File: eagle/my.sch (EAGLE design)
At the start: 15 parts, among them U1 ESP8266-01, U2 AM2301, U3 PIC12F675P, U4 U1V11F3

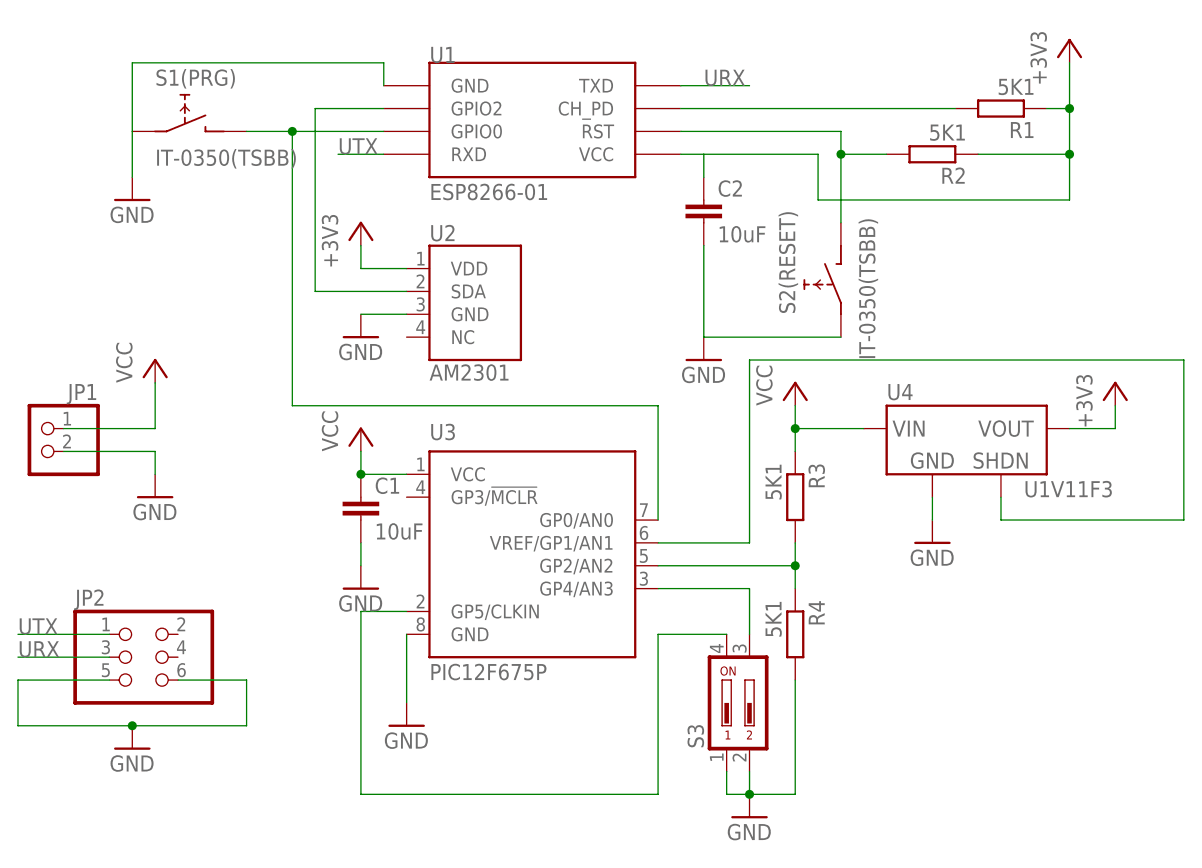
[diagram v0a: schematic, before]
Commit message: SMP components and hand-made
Switched to use SMP components and hand-made circuit board
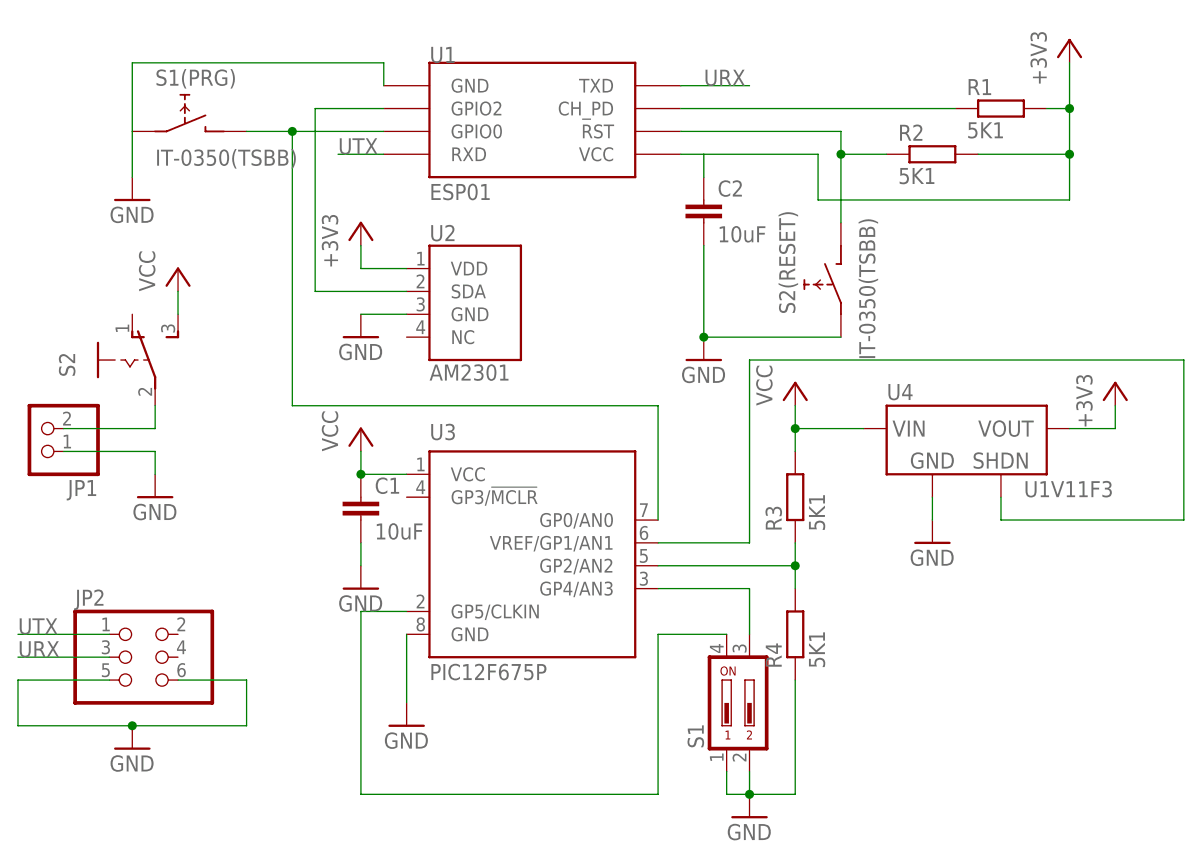
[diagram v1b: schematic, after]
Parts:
- removed S3: (no value), switch-dil:DA02
- added S1: (no value), my:DS02
- added S2: (no value), my:SS-12D00
- C1, C2: device rcl:C-EU025-025X050 -> rcl:C-EUC3216
- JP1: device pinhead:PINHD-1X2/90 -> my:PINHD-1X2/90
- JP2: device pinhead:PINHD-2X3 -> my:PINHD-2X3
- R1, R2, R3, R4: device rcl:R-EU_0207/10 -> rcl:R-EU_R3216
- U1: value ESP8266-01 -> ESP01; device esp8266modules:ESP01 -> my:ESP01
- U3: device microchip:PIC12F675P -> my:PIC12F675P
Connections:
- new net N$10: JP1.2, S2.P
- net +3V3: now also R1.2, R2.2; no longer R1.1, R2.1
- net GND: now also JP1.1, R4.1, S1.1, S1.2; no longer JP1.2, R4.2, S3.1, S3.2
- net N$1: now also R3.1, R4.2; no longer R3.2, R4.1
- net N$2: now also R2.1; no longer R2.2
- net N$5: now also S1.4; no longer S3.4
- net N$6: now also S1.3; no longer S3.3
- net N$8: now also R1.1; no longer R1.2
- net URX: now also U1.TXD
- net VCC: now also R3.2, S2.S; no longer JP1.1, R3.1
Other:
- moved on the sheet: JP1, R1, R2, R3, R4
